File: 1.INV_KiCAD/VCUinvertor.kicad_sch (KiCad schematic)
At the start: 117 parts, among them J7 PowerSupply, J9 BRAKE LIGHT, K1 IM06DGR, Q1 2N7002, Q10 2N7002, Q13 BC848C, Q2 2N7002, Q3 2N7002, Q4 2N7002, Q5 2N7002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

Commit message: Changes on NXPTPSOUT1&2
1. Switch The switch to NO from NC --> From pin 2 to pin 4
2.Move the connectors of the TPS OUT1 & 2
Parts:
- R27, R28: footprint Resistor_SMD:R_0805_2012Metric -> Resistor_SMD:R_1206_3216Metric_Pad1.30x1.75mm_HandSolder
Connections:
- net NXP_TPSOUT01: now also NXP11.4 (Pin_4); no longer NXP11.1 (Pin_1)
- net NXP_TPSOUT02: now also NXP11.1 (Pin_1); no longer NXP11.4 (Pin_4)
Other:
- note removed: "1. Switch The switch to NO from NC --> From pin 2 to pin 4 2.Move the connectors of the TPS OUT1 & 2"
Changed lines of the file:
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@@
 		)
 	)
-	(text "1. Switch The switch to NO from NC --> From pin 2 to pin 4\n2.Move the connectors of the TPS OUT1 & 2"
-		(exclude_from_sim no)
-		(at 460.756 238.506 0)
-		(effects
-			(font
-				(size 1.27 1.27)
-			)
-		)
-	)
 	(junction
 		(at 203.2 82.55)
@@
 	(wire
 		(pts
-			(xy 123.19 73.66) (xy 107.95 73.66)
-		)
-		(stroke
-			(width 0)
-			(type default)
-		)
-	)
-	(wire
-		(pts
 			(xy 107.95 102.87) (xy 143.51 102.87)
 		)
@@
 	(wire
 		(pts
+			(xy 121.92 80.01) (xy 123.19 80.01)
+		)
+		(stroke
+			(width 0)
+			(type default)
+		)
+	)
+	(wire
+		(pts
 			(xy 369.57 85.09) (xy 369.57 87.63)
 		)
@@
 	(wire
 		(pts
-			(xy 121.92 80.01) (xy 123.19 80.01)
-		)
-		(stroke
-			(width 0)
-			(type default)
-		)
-	)
-	(wire
-		(pts
 			(xy 384.81 219.71) (xy 388.62 219.71)
 		)
@@
 	(wire
 		(pts
+			(xy 107.95 73.66) (xy 123.19 73.66)
+		)
+		(stroke
+			(width 0)
+			(type default)
+		)
+	)
+	(wire
+		(pts
 			(xy 93.98 29.21) (xy 93.98 33.02)
 		)
@@
 	(global_label "NXP_TPSOUT02"
 		(shape input)
-		(at 123.19 80.01 0)
+		(at 123.19 73.66 0)
 		(fields_autoplaced yes)
 		(effects
@@
 		)
 		(property "Intersheetrefs" "${INTERSHEET_REFS}"
-			(at 140.4475 80.01 0)
+			(at 140.4475 73.66 0)
 			(hide yes)
 			(show_name no)
@@
 	(global_label "NXP_TPSOUT01"
 		(shape input)
-		(at 123.19 73.66 0)
+		(at 123.19 80.01 0)
 		(fields_autoplaced yes)
 		(effects
@@
 		)
 		(property "Intersheetrefs" "${INTERSHEET_REFS}"
-			(at 140.4475 73.66 0)
+			(at 140.4475 80.01 0)
 			(hide yes)
 			(show_name no)
@@
 			)
 		)
-		(property "Footprint" "Resistor_SMD:R_0805_2012Metric"
+		(property "Footprint" "Resistor_SMD:R_1206_3216Metric_Pad1.30x1.75mm_HandSolder"
 			(at 318.77 198.12 0)
 			(hide yes)
@@
 			)
 		)
-		(property "Footprint" "Resistor_SMD:R_0805_2012Metric"
+		(property "Footprint" "Resistor_SMD:R_1206_3216Metric_Pad1.30x1.75mm_HandSolder"
 			(at 318.77 207.01 0)
 			(hide yes)

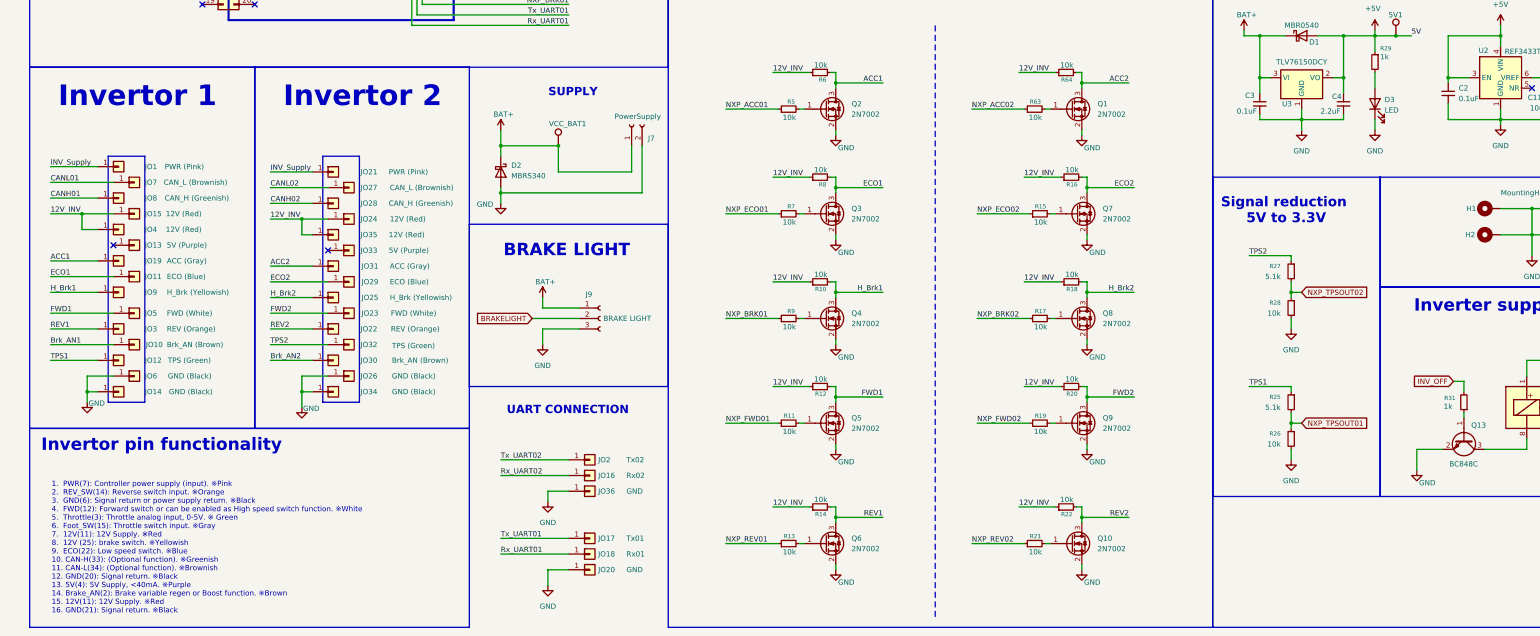
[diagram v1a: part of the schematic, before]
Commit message: MOS pulldown + missing INV pins added
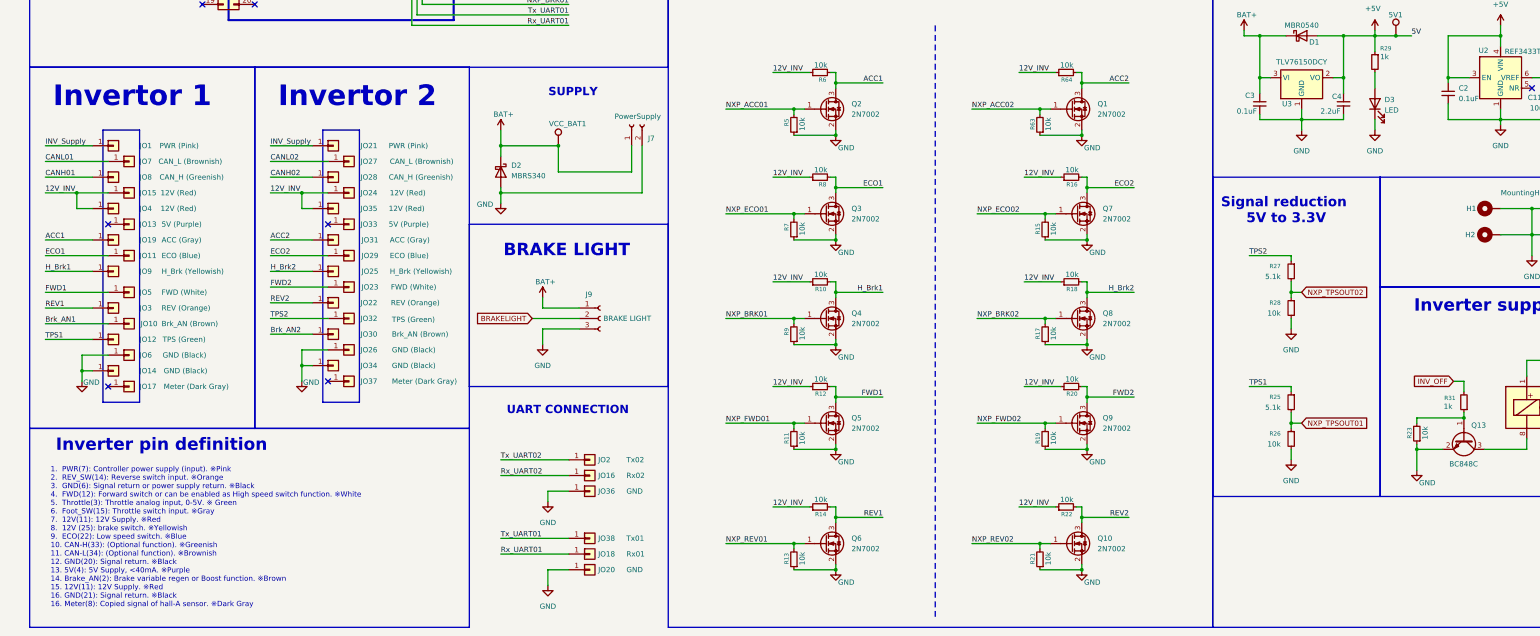
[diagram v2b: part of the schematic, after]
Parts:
- added JO17, JO37: Meter (Dark Gray), Connector_Wire:SolderWire-0.75sqmm_1x01_D1.25mm_OD2.3mm, symbol Connector_Generic:Conn_01x01
- added R23: 10k, Resistor_SMD:R_1206_3216Metric_Pad1.30x1.75mm_HandSolder, symbol Device:R_Small
- renumbered JO17 to JO38
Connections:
- net GND: now also R11.1, R13.1, R15.1, R17.1, R19.1, R21.1, R5.1, R63.1, R7.1, R9.1, R23.1
- net NXP_ACC01: now also Q2.1 (G), R5.2; no longer R5.1
- net NXP_ACC02: now also Q1.1 (G), R63.2; no longer R63.1
- net NXP_BRK01: now also Q4.1 (G), R9.2; no longer R9.1
- net NXP_BRK02: now also Q8.1 (G), R17.2; no longer R17.1
- net NXP_ECO01: now also Q3.1 (G), R7.2; no longer R7.1
- net NXP_ECO02: now also Q7.1 (G), R15.2; no longer R15.1
- net NXP_FWD01: now also Q5.1 (G), R11.2; no longer R11.1
- net NXP_FWD02: now also Q9.1 (G), R19.2; no longer R19.1
- net NXP_REV01: now also Q6.1 (G), R13.2; no longer R13.1
- net NXP_REV02: now also Q10.1 (G), R21.2; no longer R21.1
- net at Q13.1 (B), R31.1: now also R23.2
- no-connect marks 88 -> 90
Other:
- note added: "Inverter pin definition"
- note removed: "Invertor pin functionality"
- moved on the sheet: JO1, JO10, JO11, JO12, JO13, JO14, JO15, JO19, JO21, JO22, JO23, JO24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

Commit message: Wire labels correction
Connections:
- net RX0 renamed RX2
- net TX0 renamed TX2
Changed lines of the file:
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@@
 		)
 	)
-	(label "RX0"
+	(label "RX2"
 		(at 251.46 85.09 0)
 		(effects
@@
 		)
 	)
-	(label "RX0"
+	(label "RX2"
 		(at 139.7 40.64 180)
 		(effects
@@
 		)
 	)
-	(label "TX0"
+	(label "TX2"
 		(at 139.7 38.1 180)
 		(effects
@@
 		)
 	)
-	(label "TX0"
+	(label "TX2"
 		(at 251.46 82.55 0)
 		(effects
@@
 		)
 		(property "Value" "NXP12"
-			(at 126.238 128.27 0)
+			(at 111.76 132.08 0)
 			(show_name no)
 			(do_not_autoplace no)
@@
 		)
 		(property "Value" "NXP13"
-			(at 64.77 71.374 0)
+			(at 64.516 47.752 0)
 			(show_name no)
 			(do_not_autoplace no)

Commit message: Revision author added
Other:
- company: (none) -> EVR TUIASI
- title: (none) -> Shield Invertoare - STEPULEAC GHEORGHE

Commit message: Corrections + PUMP&FAN circuit 0.1
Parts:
- added D5, D6, D7, D8: SS34, Diode_SMD:D_SMA, symbol Diode:SS34
- added J10: FAN2, Connector_JST:JST_PH_B2B-PH-K_1x02_P2.00mm_Vertical, symbol Connector:Conn_01x02_Socket
- added J11: PUMP1, Connector_JST:JST_PH_B2B-PH-K_1x02_P2.00mm_Vertical, symbol Connector:Conn_01x02_Socket
- added J12: PUMP2, Connector_JST:JST_PH_B2B-PH-K_1x02_P2.00mm_Vertical, symbol Connector:Conn_01x02_Socket
- added J8: FAN1, Connector_JST:JST_PH_B2B-PH-K_1x02_P2.00mm_Vertical, symbol Connector:Conn_01x02_Socket
- added Q11: 2N7002, Package_TO_SOT_SMD:SOT-23, symbol Transistor_FET:2N7002
- added Q15, Q16, Q17, Q18: IRLZ44N, Package_TO_SOT_THT:TO-220-3_Vertical, symbol Transistor_FET:IRLZ44N
- added R34, R36, R38: 100, Resistor_SMD:R_1206_3216Metric_Pad1.30x1.75mm_HandSolder, symbol Device:R_Small
- added R35, R37, R39, R40: 100k, Resistor_SMD:R_1206_3216Metric_Pad1.30x1.75mm_HandSolder, symbol Device:R_Small
- added R41: 47k, Resistor_SMD:R_1206_3216Metric_Pad1.30x1.75mm_HandSolder, symbol Device:R_Small
- added R42: 100R, Resistor_SMD:R_1206_3216Metric_Pad1.30x1.75mm_HandSolder, symbol Device:R_Small
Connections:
- net +5V: no longer U2.3 (EN)
- net BAT+: now also K1.5, D7.1 (K), J10.1 (Pin_1), J11.1 (Pin_1), J12.1 (Pin_1), J8.1 (Pin_1), R41.2
- net GND: now also U2.3 (EN), U2.5 (NR), Q11.2 (S), Q15.2 (D), Q16.2 (D), Q17.2 (D), Q18.2 (D), R35.1, R37.1, R39.1, R40.1
- net Pyy: now also NXP10.16 (Pin_16); no longer NXP10.18 (Pin_18)
- net RX1: now also NXP10.1 (Pin_1); no longer NXP10.13 (Pin_13)
- net TX1: now also NXP10.18 (Pin_18); no longer NXP10.15 (Pin_15)
- net INV1_VCC: now reaches K1.6
- net INV1_VCC: now also JO1.1 (Pin_1)
- net INV_Supply renamed INV2_VCC
- net INV2_VCC: no longer JO1.1 (Pin_1)
- new net: J10.2 (Pin_2), Q16.3 (S)
- new net: Q18.1 (G), R38.1, R39.2
- new net: Q17.1 (G), R36.1, R37.2
- new net: D7.2 (A), J8.2 (Pin_2), Q15.3 (S)
- new net: Q11.1 (G), R40.2, R42.2
- new net: Q11.3 (D), Q15.1 (G), R41.1
- new net: J11.2 (Pin_2), Q17.3 (S)
- new net: J12.2 (Pin_2), Q18.3 (S)
- new net: Q16.1 (G), R34.1, R35.2
- new net FAN1: R42.1
- new net FAN2: R34.2
- new net PUMP1: R36.2
- new net PUMP2: R38.2
- no-connect marks 90 -> 86
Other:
- note added: "FAN&PUMP CONTROL"
- moved on the sheet: 5V1, C11, C2, C3, C4, D1, D3, K1, Q1, Q10, Q13, Q2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

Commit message: PCB Layout with FAN&PUMP MOS - Done
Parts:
- removed D5, D6: SS34, Diode_SMD:D_SMA, symbol Diode:SS34
- removed Q18: IRLZ44N, Package_TO_SOT_THT:TO-220-3_Vertical, symbol Transistor_FET:IRLZ44N
- removed R34, R36, R38: 100, Resistor_SMD:R_1206_3216Metric_Pad1.30x1.75mm_HandSolder, symbol Device:R_Small
- removed R35, R37, R39: 100k, Resistor_SMD:R_1206_3216Metric_Pad1.30x1.75mm_HandSolder, symbol Device:R_Small
- added D10, D9: SS34, Diode_SMD:D_SMA, symbol Diode:SS34
- added Q12, Q14, Q18: 2N7002, Package_TO_SOT_SMD:SOT-23, symbol Transistor_FET:2N7002
- added Q19: IRLZ44N, Package_TO_SOT_THT:TO-220-3_Vertical, symbol Transistor_FET:IRLZ44N
- added R43, R46, R49: 100R, Resistor_SMD:R_1206_3216Metric_Pad1.30x1.75mm_HandSolder, symbol Device:R_Small
- added R44: 10k, Resistor_SMD:R_1206_3216Metric_Pad1.30x1.75mm_HandSolder, symbol Device:R_Small
- added R45, R48, R51: 47k, Resistor_SMD:R_1206_3216Metric_Pad1.30x1.75mm_HandSolder, symbol Device:R_Small
- added R47, R50: 100k, Resistor_SMD:R_1206_3216Metric_Pad1.30x1.75mm_HandSolder, symbol Device:R_Small
- added R52, R53, R54, R55, R56, R57, R58, R59, R60, R61: 100R, Resistor_SMD:R_0805_2012Metric, symbol Device:R_Small
- R11, R15, R17, R19, R5, R63, R7, R9: value 10k -> 100k
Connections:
- net BAT+: now also D8.1 (K), D10.1 (K), D9.1 (K), R45.2, R48.2, R51.2
- net FAN2: now also R43.1
- net GND: now also Q12.2 (S), Q14.2 (S), Q18.2 (S), Q19.2 (D), R44.1, R47.1, R50.1
- net NXP_ACC01: now also R52.1; no longer Q2.1 (G), R5.2
- net NXP_ACC02: now also R60.1; no longer Q1.1 (G), R63.2
- net NXP_BRK01: now also R54.1; no longer Q4.1 (G), R9.2
- net NXP_BRK02: now also R58.1; no longer Q8.1 (G), R17.2
- net NXP_ECO01: now also R53.1; no longer Q3.1 (G), R7.2
- net NXP_ECO02: now also R59.1; no longer Q7.1 (G), R15.2
- net NXP_FWD01: now also R55.1; no longer Q5.1 (G), R11.2
- net NXP_FWD02: now also R61.1; no longer Q9.1 (G), R19.2
- net NXP_REV01: now also R56.1; no longer Q6.1 (G), R13.2
- net NXP_REV02: now also R57.1; no longer Q10.1 (G), R21.2
- net PUMP1: now also R46.1
- net PUMP2: now also R49.1
- net at J10.2 (Pin_2), Q16.3 (S): now also D8.2 (A)
- net at Q17.1 (G): now also Q14.3 (D), R48.1
- net at J11.2 (Pin_2), Q17.3 (S): now also D9.2 (A)
- net at J12.2 (Pin_2): now also D10.2 (A), Q19.3 (S)
- net at Q16.1 (G): now also Q12.3 (D), R45.1
- new net: Q7.1 (G), R15.2, R59.2
- new net: Q6.1 (G), R13.2, R56.2
- new net: Q1.1 (G), R60.2, R63.2
- new net: Q12.1 (G), R43.2, R44.2
- new net: Q9.1 (G), R19.2, R61.2
- new net: Q18.1 (G), R49.2, R50.2
- new net: Q5.1 (G), R11.2, R55.2
- new net: Q18.3 (D), Q19.1 (G), R51.1
- new net: Q4.1 (G), R54.2, R9.2
- new net: Q3.1 (G), R53.2, R7.2
- new net: Q14.1 (G), R46.2, R47.2
- new net: Q2.1 (G), R5.2, R52.2
- new net: Q10.1 (G), R21.2, R57.2
- new net: Q8.1 (G), R17.2, R58.2
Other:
- moved on the sheet: 3.3V1, 5V1, C1, C10, C11, C12, C2, C3, C4, C5, C6, C7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

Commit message: INV pinout+ layout changes - Done
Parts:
- added R24: 100k, Resistor_SMD:R_1206_3216Metric_Pad1.30x1.75mm_HandSolder, symbol Device:R_Small
- J7: footprint Connector_JST:JST_PH_B2B-PH-K_1x02_P2.00mm_Vertical -> Connector_Phoenix_GMSTB:PhoenixContact_GMSTBVA_2,5_2-G-7,62_1x02_P7.62mm_Vertical
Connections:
- net +3.3V: no longer DAC1.9 (*PD)
- net FAN1: now also NXP13.11 (Pin_11)
- net FAN2: now also NXP13.9 (Pin_9)
- net GND: now also R24.2
- net NXP_ACC02: now also NXP12.17 (Pin_17); no longer NXP12.20 (Pin_20)
- net NXP_TPSOUT01: now also NXP11.3 (Pin_3); no longer NXP11.4 (Pin_4)
- net NXP_TPSOUT02: now also NXP11.5 (Pin_5); no longer NXP11.1 (Pin_1)
- net PUMP1: now also NXP13.7 (Pin_7)
- net PUMP2: now also NXP13.5 (Pin_5)
- net Pyy: now also NXP10.12 (Pin_12); no longer NXP10.16 (Pin_16)
- net Rx_UART02: now also NXP12.20 (Pin_20); no longer NXP11.2 (Pin_2)
- net Tx_UART02: now also NXP12.19 (Pin_19); no longer NXP11.3 (Pin_3)
- net DAC_PD: now reaches NXP11.8 (Pin_8)
- net DAC_PD: now also DAC1.9 (*PD), R24.1
- no-connect marks 86 -> 81
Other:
- moved on the sheet: C1

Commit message: Board silkscreen corrections for visibility
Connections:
- net INV1_VCC renamed INV1_Vcc
- net INV2_VCC renamed INV2_Vcc
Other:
- moved on the sheet: JO1, JO10, JO11, JO12, JO13, JO14, JO15, JO17, JO19, JO3, JO4, JO5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
